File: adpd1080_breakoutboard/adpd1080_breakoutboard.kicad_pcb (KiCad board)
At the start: 2 copper layers, 47 x 39 mm, 30 parts, among them IC1 ADPD1080BCPZR7, J1 1V8_IN, J2 3V3_IN, J3 PG_TP, J4 P_05, J5 P_01, J6 PD_7, J7 P_3_LED, J8 P_1, U1 LD39100 1V8, U2 TXB0104PW_new

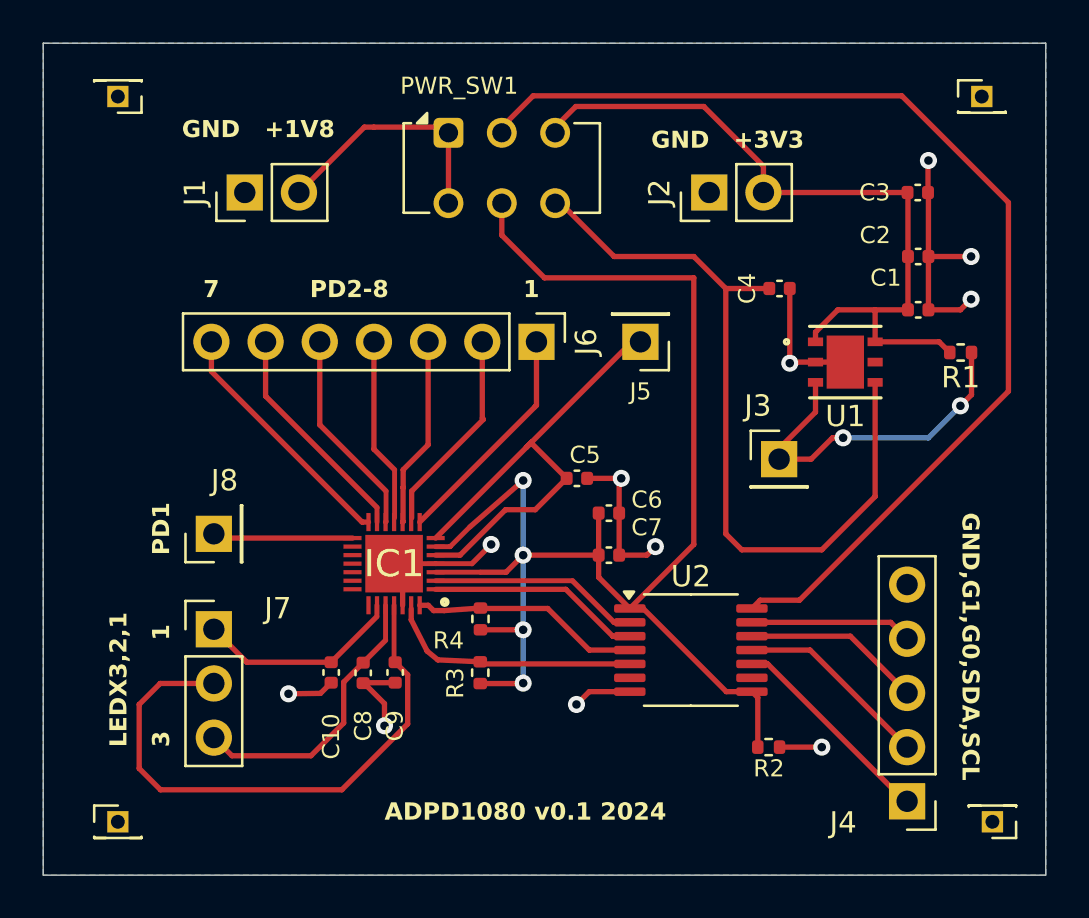
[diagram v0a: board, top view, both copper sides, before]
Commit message: removed caps that were in wrong side of ledx
Signed-off-by: Mika Laitio <lamikr@gmail.com>
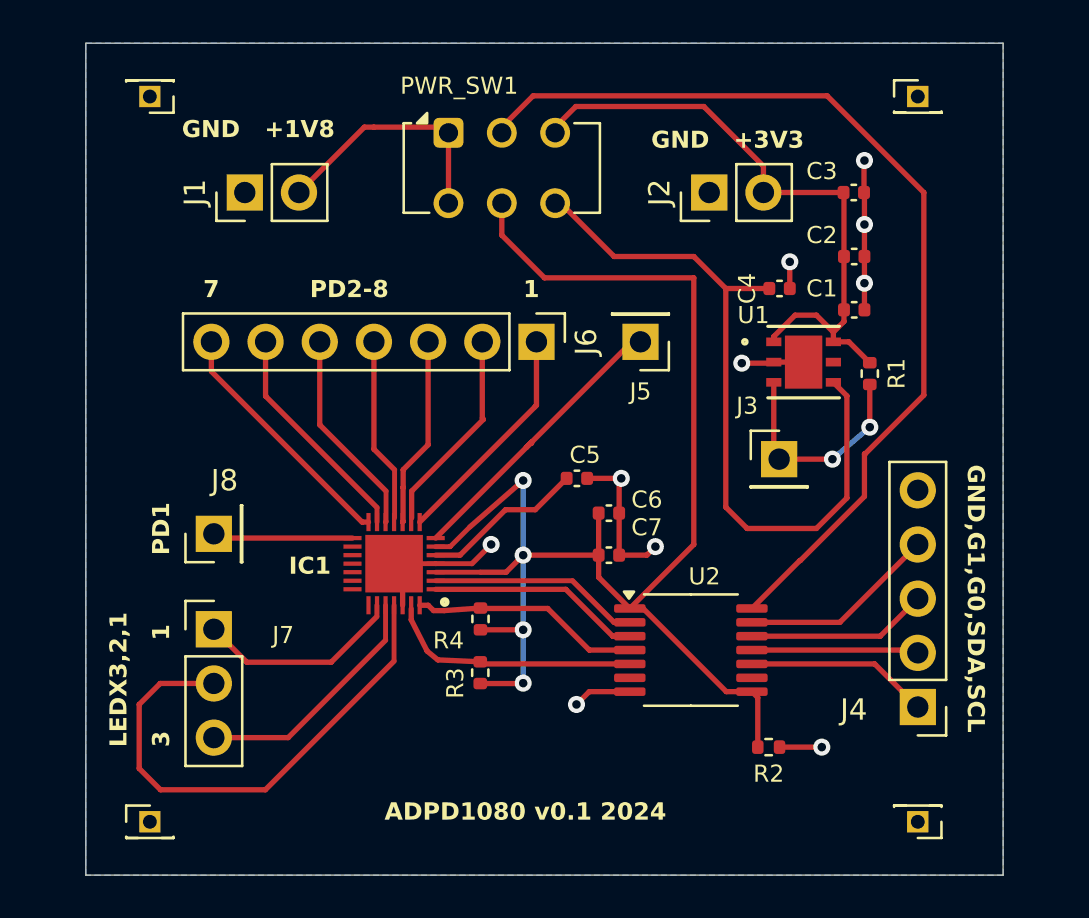
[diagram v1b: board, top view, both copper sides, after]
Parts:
- removed C10, C8, C9: 4.7u, Capacitor_SMD:C_0402_1005Metric
- moved J4 4.45 mm to (59.0, 51.1)
- moved R1 4.37 mm to (56.8, 35.5), turned to 90 degrees
- moved H3 3.50 mm to (59.0, 56.5)
- moved C1 3.00 mm to (56.0, 32.5)
- moved C2 3.00 mm to (56.0, 30.0)
- moved C3 3.00 mm to (56.0, 27.0)
- moved H2 3.00 mm to (59.0, 22.5)
- moved U1 1.96 mm to (53.6, 35.0)
- moved H1 1.50 mm to (23.0, 22.5)
- moved H4 1.50 mm to (23.0, 56.5)
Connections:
- C5 pad 1: Net-(IC1-PD1) -> Net-(IC1-VREF)
- IC1 pad 5: Net-(IC1-PD1) -> Net-(IC1-VREF)
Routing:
- net GND: track 41.8 -> 29.6 mm, vias 11 -> 10
- net Net-(IC1-PD1): track 23.8 -> 13.8 mm
- net Net-(IC1-VREF): track 0.00 -> 7.63 mm
- net VDD_INPUT: track 51.5 -> 45.1 mm
- net Net-(J2-Pin_2): track 35.3 -> 29.4 mm
- net Net-(J3-Pin_1): track 16.6 -> 11.0 mm
- net Net-(IC1-LEDX2): track 27.0 -> 24.4 mm
- net Net-(U1-VOUT): track 37.0 -> 34.4 mm
- net Net-(IC1-LEDX3): track 13.4 -> 11.6 mm
- net Net-(J4-Pin_4): track 7.59 -> 9.29 mm
- net Net-(J4-Pin_2): track 9.16 -> 7.83 mm
- net Net-(J4-Pin_1): track 9.94 -> 8.61 mm
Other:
- board size 47 x 39 mm -> 43 x 39 mm
